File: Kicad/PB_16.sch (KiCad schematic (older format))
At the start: 27 parts, among them J17 Power In Left, J18 Power In Right, J19 USB, J23 VIN_Voltage, J24 Expansion Header, J25 RTC Conn, J26 OLED Select, J27 GPIO Header, J28 Aux Pwr, J29 VIN_Select, SW2 OLED Select, U2 LM7805

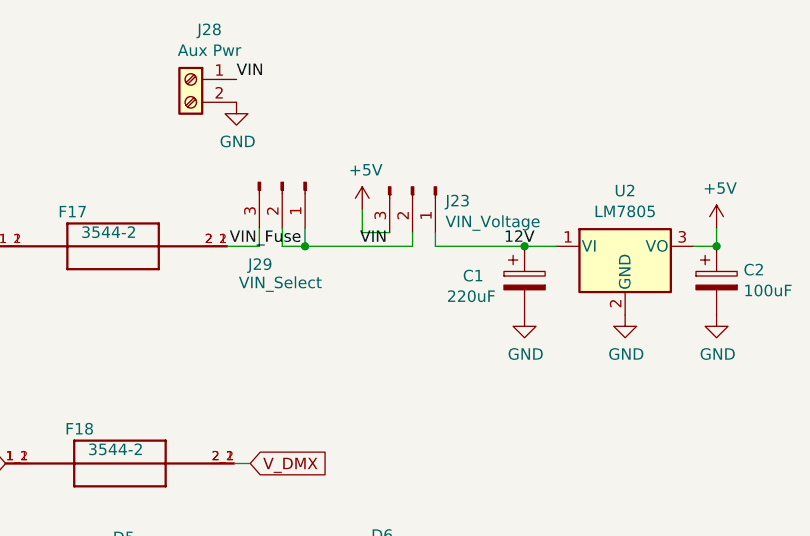
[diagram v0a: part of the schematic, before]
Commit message: updated Aux header to 3.81mm spaced header
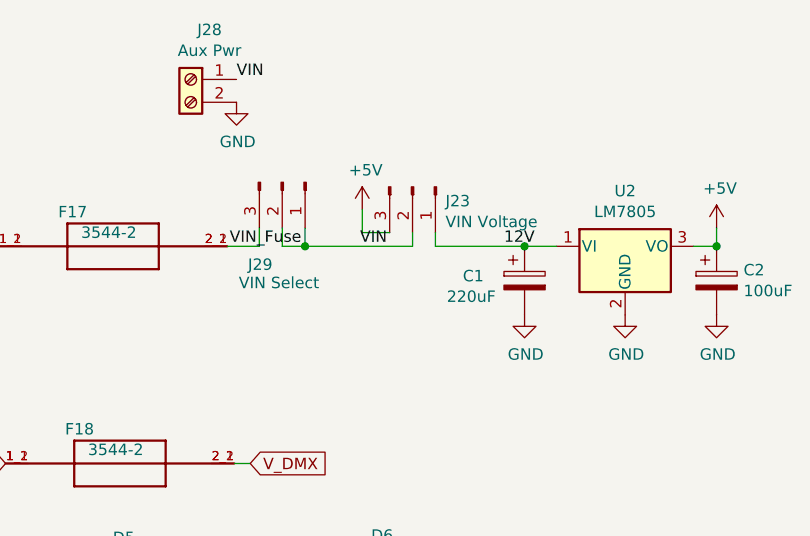
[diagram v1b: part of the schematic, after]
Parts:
- J23: value VIN_Voltage -> VIN Voltage
- J28: footprint TerminalBlock_TE-Connectivity:TerminalBlock_TE_282834-2_1x02_P2.54mm_Horizontal -> TerminalBlock_MetzConnect:TerminalBlock_MetzConnect_Type086_RT03402HBLC_1x02_P3.81mm_Horizontal; Digi-Key_PN A98333-ND -> 277-1947-ND; MPN 282834-2 -> 1727010
- J29: value VIN_Select -> VIN Select
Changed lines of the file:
@@
 EESchema Schematic File Version 4
 LIBS:PB_16-cache
-EELAYER 29 0
+EELAYER 30 0
 EELAYER END
 $Descr A4 11693 8268
@@
 Sheet 1 5
 Title "PB 16"
-Date "2019-08-24"
-Rev "v1.0d"
+Date "2019-09-19"
+Rev "v1.0e"
 Comp "Scott Hanson"
 Comment1 ""
@@
 P 7830 1330
 F 0 "J23" V 7892 1474 50  0000 L CNN
-F 1 "VIN_Voltage" V 7983 1474 50  0000 L CNN
+F 1 "VIN Voltage" V 7983 1474 50  0000 L CNN
 F 2 "Connector_PinHeader_2.54mm:PinHeader_1x03_P2.54mm_Vertical" H 7830 1330 50  0001 C CNN
 F 3 "~" H 7830 1330 50  0001 C CNN
@@
 F 0 "J28" H 6778 1077 50  0000 C CNN
 F 1 "Aux Pwr" H 6778 986 50  0000 C CNN
-F 2 "TerminalBlock_TE-Connectivity:TerminalBlock_TE_282834-2_1x02_P2.54mm_Horizontal" H 6860 860 50  0001 C CNN
+F 2 "TerminalBlock_MetzConnect:TerminalBlock_MetzConnect_Type086_RT03402HBLC_1x02_P3.81mm_Horizontal" H 6860 860 50  0001 C CNN
 F 3 "~" H 6860 860 50  0001 C CNN
-F 4 "A98333-ND" H 6860 860 50  0001 C CNN "Digi-Key_PN"
-F 5 "282834-2" H 6860 860 50  0001 C CNN "MPN"
+F 4 "277-1947-ND" H 6860 860 50  0001 C CNN "Digi-Key_PN"
+F 5 "1727010" H 6860 860 50  0001 C CNN "MPN"
 	1    6860 860
 	-1   0    0    -1
@@
 P 7260 1310
 F 0 "J29" V 7620 1160 50  0000 L CNN
-F 1 "VIN_Select" V 7700 1120 50  0000 L CNN
+F 1 "VIN Select" V 7700 1120 50  0000 L CNN
 F 2 "Connector_PinHeader_2.54mm:PinHeader_1x03_P2.54mm_Vertical" H 7260 1310 50  0001 C CNN
 F 3 "~" H 7260 1310 50  0001 C CNN

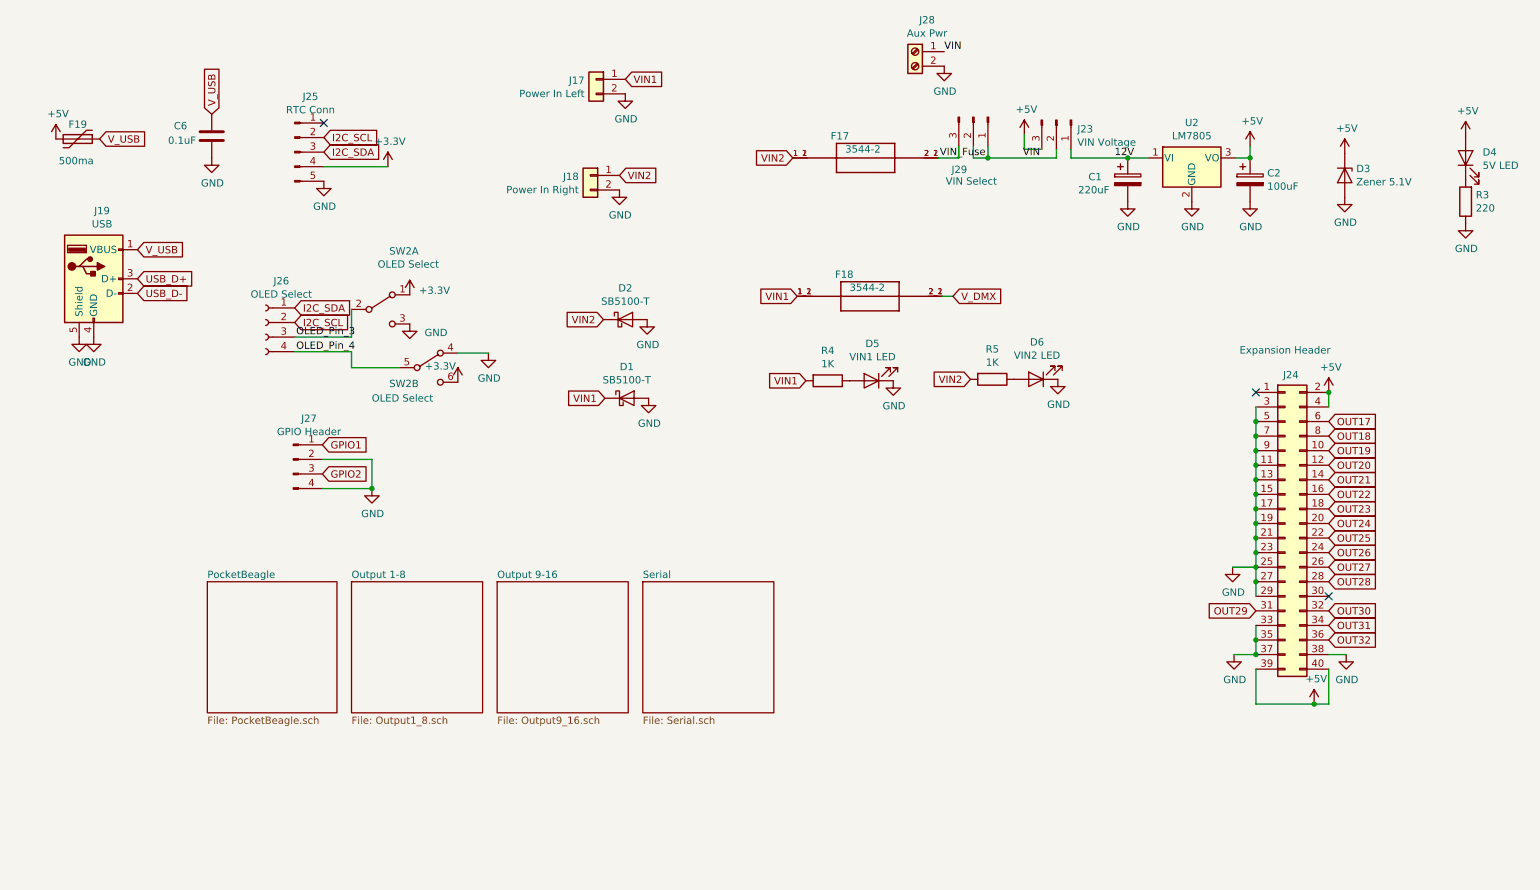
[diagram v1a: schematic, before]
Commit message: Added LOR/DMX Serial Port Selector, EEPROM, and Push buttons
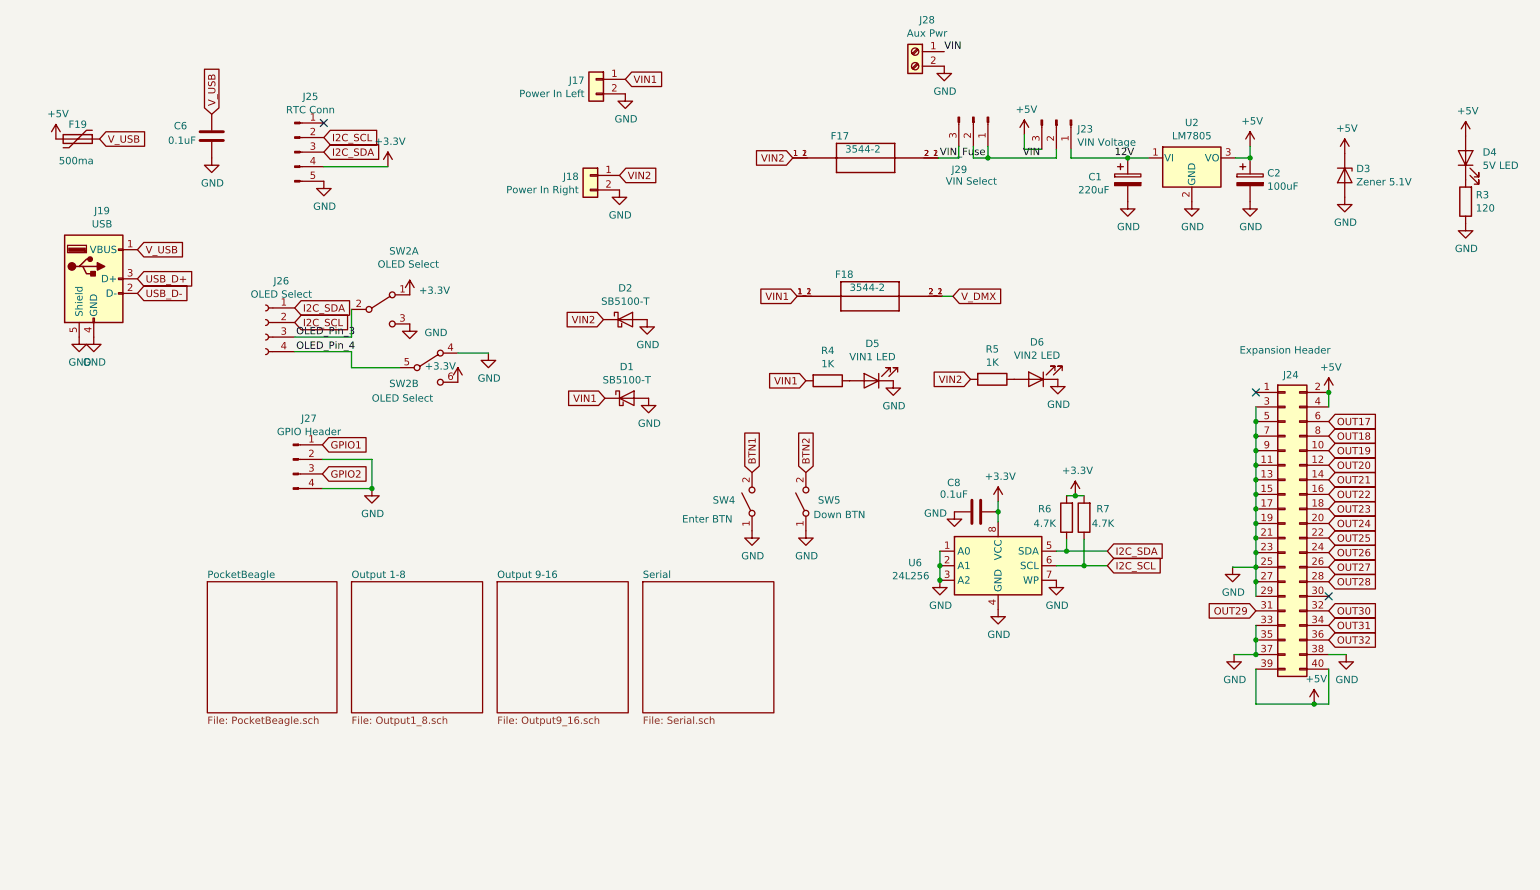
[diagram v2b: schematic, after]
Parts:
- added C8: 0.1uF, Capacitor_THT:C_Rect_L7.0mm_W2.0mm_P5.00mm, symbol Device:C
- added R6, R7: 4.7K, Resistor_THT:R_Axial_DIN0207_L6.3mm_D2.5mm_P7.62mm_Horizontal, symbol Device:R
- added SW4: Enter BTN, Button_Switch_THT:SW_PUSH_6mm, symbol Switch:SW_SPST
- added SW5: Down BTN, Button_Switch_THT:SW_PUSH_6mm, symbol Switch:SW_SPST
- added U6: 24L256, Package_DIP:DIP-8_W7.62mm, symbol Memory_EEPROM:24LC32
- D4, D5, D6: footprint LED_THT:LED_D3.0mm -> LED_THT:LED_D3.0mm_Clear
- R3: value 220 -> 120; Digi-Key_PN CF14JT220RCT-ND -> CF14JT120RCT-ND; MPN CF14JT220R -> CF14JT120R
- U2: footprint Package_TO_SOT_THT:TO-220-3_Horizontal_TabDown -> Package_TO_SOT_THT:TO-220-3_Vertical
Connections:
- net +3V3: now also C8.1, R6.2, R7.2, U6.8 (VCC)
- net GND: now also C8.2, SW4.1 (A), SW5.1 (A), U6.1 (A0), U6.2 (A1), U6.3 (A2), U6.4 (GND), U6.7 (WP)
- net I2C_SCL: now also R7.1, U6.6 (SCL)
- net I2C_SDA: now also R6.1, U6.5 (SDA)
- new net BTN1: SW4.2 (B)
- new net BTN2: SW5.2 (B)
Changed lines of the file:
@@
 Sheet 1 5
 Title "PB 16"
-Date "2019-09-19"
-Rev "v1.0e"
+Date "2019-10-07"
+Rev "v1.0f"
 Comp "Scott Hanson"
 Comment1 ""
@@
 F 0 "U2" H 8760 1832 50  0000 C CNN
 F 1 "LM7805" H 8760 1741 50  0000 C CNN
-F 2 "Package_TO_SOT_THT:TO-220-3_Horizontal_TabDown" H 8760 1815 50  0001 C CIN
+F 2 "Package_TO_SOT_THT:TO-220-3_Vertical" H 8760 1815 50  0001 C CIN
 F 3 "http://www.fairchildsemi.com/ds/LM/LM7805.pdf" H 8760 1540 50  0001 C CNN
 F 4 "811-2196-5-ND" H -340 -170 50  0001 C CNN "Digi-Key_PN"
@@
 F 0 "D5" H 6553 2865 50  0000 C CNN
 F 1 "VIN1 LED" H 6553 2956 50  0000 C CNN
-F 2 "LED_THT:LED_D3.0mm" H 6560 3120 50  0001 C CNN
+F 2 "LED_THT:LED_D3.0mm_Clear" H 6560 3120 50  0001 C CNN
 F 3 "~" H 6560 3120 50  0001 C CNN
 F 4 "754-1217-ND" H 6560 3120 50  0001 C CNN "Digi-Key_PN"
@@
 P 10640 1890
 F 0 "R3" H 10570 1844 50  0000 R CNN
-F 1 "220" H 10570 1935 50  0000 R CNN
+F 1 "120" H 10570 1935 50  0000 R CNN
 F 2 "Resistor_THT:R_Axial_DIN0207_L6.3mm_D2.5mm_P7.62mm_Horizontal" V 10570 1890 50  0001 C CNN
 F 3 "~" H 10640 1890 50  0001 C CNN
-F 4 "CF14JT220RCT-ND" H 10640 1890 50  0001 C CNN "Digi-Key_PN"
-F 5 "CF14JT220R" H 10640 1890 50  0001 C CNN "MPN"
+F 4 "CF14JT120RCT-ND" H 10640 1890 50  0001 C CNN "Digi-Key_PN"
+F 5 "CF14JT120R" H 10640 1890 50  0001 C CNN "MPN"
 	1    10640 1890
 	-1   0    0    1
@@
 F 0 "D6" H 7683 2855 50  0000 C CNN
 F 1 "VIN2 LED" H 7683 2946 50  0000 C CNN
-F 2 "LED_THT:LED_D3.0mm" H 7690 3110 50  0001 C CNN
+F 2 "LED_THT:LED_D3.0mm_Clear" H 7690 3110 50  0001 C CNN
 F 3 "~" H 7690 3110 50  0001 C CNN
 F 4 "754-1217-ND" H 7690 3110 50  0001 C CNN "Digi-Key_PN"
@@
 F 0 "D4" V 10679 1473 50  0000 R CNN
 F 1 "5V LED" V 10588 1473 50  0000 R CNN
-F 2 "LED_THT:LED_D3.0mm" H 10640 1590 50  0001 C CNN
+F 2 "LED_THT:LED_D3.0mm_Clear" H 10640 1590 50  0001 C CNN
 F 3 "~" H 10640 1590 50  0001 C CNN
 F 4 "754-1217-ND" H 10640 1590 50  0001 C CNN "Digi-Key_PN"
@@
 Wire Wire Line
 	7360 1510 7360 1590
+$Comp
+L Memory_EEPROM:24LC32 U6
+U 1 1 5D915A6B
+P 7430 4390
+F 0 "U6" H 6860 4410 50  0000 C CNN
+F 1 "24L256" H 6830 4320 50  0000 C CNN
+F 2 "Package_DIP:DIP-8_W7.62mm" H 7430 4390 50  0001 C CNN
+F 3 "http://ww1.microchip.com/downloads/en/DeviceDoc/21072G.pdf" H 7430 4390 50  0001 C CNN
+F 4 "1219-1052-ND" H 7430 4390 50  0001 C CNN "Digi-Key_PN"
+F 5 "FT24C256A-UDR-B" H 7430 4390 50  0001 C CNN "MPN"
+	1    7430 4390
+	1    0    0    -1
+$EndComp
+$Comp
+L power:GND #PWR059
+U 1 1 5D917DF1
+P 7830 4490
+F 0 "#PWR059" H 7830 4240 50  0001 C CNN
+F 1 "GND" H 7835 4317 50  0000 C CNN
+F 2 "" H 7830 4490 50  0001 C CNN
+F 3 "" H 7830 4490 50  0001 C CNN
+	1    7830 4490
+	1    0    0    -1
+$EndComp
+Text GLabel 8180 4390 2    50   Input ~ 0
+I2C_SCL
+Text GLabel 8180 4290 2    50   Input ~ 0
+I2C_SDA
+$Comp
+L power:+3.3V #PWR?
+U 1 1 5D918D0A
+P 7430 3950
+AR Path="/5D413C25/5D918D0A" Ref="#PWR?"  Part="1"
+AR Path="/5D918D0A" Ref="#PWR057"  Part="1"
+F 0 "#PWR057" H 7430 3800 50  0001 C CNN
+F 1 "+3.3V" H 7445 4123 50  0000 C CNN
+F 2 "" H 7430 3950 50  0001 C CNN
+F 3 "" H 7430 3950 50  0001 C CNN
+	1    7430 3950
+	1    0    0    -1
+$EndComp
+$Comp
+L power:GND #PWR058
+U 1 1 5D91A827
+P 7430 4690
+F 0 "#PWR058" H 7430 4440 50  0001 C CNN
+F 1 "GND" H 7435 4517 50  0000 C CNN
+F 2 "" H 7430 4690 50  0001 C CNN
+F 3 "" H 7430 4690 50  0001 C CNN
+	1    7430 4690
+	1    0    0    -1
+$EndComp
+$Comp
+L power:GND #PWR056
+U 1 1 5D91AC52
+P 7130 4020
+F 0 "#PWR056" H 7130 3770 50  0001 C CNN
+F 1 "GND" H 7000 4010 50  0000 C CNN
+F 2 "" H 7130 4020 50  0001 C CNN
+F 3 "" H 7130 4020 50  0001 C CNN
+	1    7130 4020
+	1    0    0    -1
+$EndComp
+Wire Wire Line
+	7030 4290 7030 4390
+Connection ~ 7030 4390
+Wire Wire Line
+	7030 4390 7030 4490
+Wire Wire Line
+	7830 4290 7900 4290
+Wire Wire Line
+	8180 4390 8020 4390
+$Comp
+L Device:C C?
+U 1 1 5D91E5B7
+P 7280 4020
+AR Path="/5D413C25/5D91E5B7" Ref="C?"  Part="1"
+AR Path="/5D91E5B7" Ref="C8"  Part="1"
+F 0 "C8" V 7080 3820 50  0000 L CNN
+F 1 "0.1uF" V 7160 3770 50  0000 L CNN
+F 2 "Capacitor_THT:C_Rect_L7.0mm_W2.0mm_P5.00mm" H 7318 3870 50  0001 C CNN
+F 3 "~" H 7280 4020 50  0001 C CNN
+F 4 "478-7336-1-ND" H 7280 4020 50  0001 C CNN "Digi-Key_PN"
+F 5 "SR215C104KARTR1" H 7280 4020 50  0001 C CNN "MPN"
+	1    7280 4020
+	0    1    1    0
+$EndComp
+Wire Wire Line
+	7430 4090 7430 4020
+Connection ~ 7430 4020
+Wire Wire Line
+	7430 4020 7430 3950
+$Comp
+L Device:R R6
+U 1 1 5D925D1A
+P 7900 4060
+F 0 "R6" H 8050 4000 50  0000 C CNN
+F 1 "4.7K" H 8050 4100 50  0000 C CNN
+F 2 "Resistor_THT:R_Axial_DIN0207_L6.3mm_D2.5mm_P7.62mm_Horizontal" V 7830 4060 50  0001 C CNN
+F 3 "~" H 7900 4060 50  0001 C CNN
+F 4 "CF14JT4K70CT-ND" H 7900 4060 50  0001 C CNN "Digi-Key_PN"
+F 5 "CF14JT4K70" H 7900 4060 50  0001 C CNN "MPN"
+	1    7900 4060
+	-1   0    0    1
+$EndComp
+$Comp
+L Device:R R7
+U 1 1 5D9267BC
+P 8020 4060
+F 0 "R7" H 7890 4000 50  0000 C CNN
+F 1 "4.7K" H 7890 4100 50  0000 C CNN
+F 2 "Resistor_THT:R_Axial_DIN0207_L6.3mm_D2.5mm_P7.62mm_Horizontal" V 7950 4060 50  0001 C CNN
+F 3 "~" H 8020 4060 50  0001 C CNN
+F 4 "CF14JT4K70CT-ND" H 8020 4060 50  0001 C CNN "Digi-Key_PN"
+F 5 "CF14JT4K70" H 8020 4060 50  0001 C CNN "MPN"
+	1    8020 4060
+	-1   0    0    1
+$EndComp
+$Comp
+L power:+3.3V #PWR?
+U 1 1 5D926B37
+P 7960 3910
+AR Path="/5D413C25/5D926B37" Ref="#PWR?"  Part="1"
+AR Path="/5D926B37" Ref="#PWR060"  Part="1"
+F 0 "#PWR060" H 7960 3760 50  0001 C CNN
+F 1 "+3.3V" H 7975 4083 50  0000 C CNN
+F 2 "" H 7960 3910 50  0001 C CNN
+F 3 "" H 7960 3910 50  0001 C CNN
+	1    7960 3910
+	1    0    0    -1
+$EndComp
+Wire Wire Line
+	7900 3910 7960 3910
+Connection ~ 7960 3910
+Wire Wire Line
+	7960 3910 8020 3910
+Wire Wire Line
+	7900 4210 7900 4290
+Connection ~ 7900 4290
+Wire Wire Line
+	7900 4290 8180 4290
+Wire Wire Line
+	8020 4210 8020 4390
+Connection ~ 8020 4390
+Wire Wire Line
+	8020 4390 7830 4390
+$Comp
+L power:GND #PWR0118
+U 1 1 5D92B95E
+P 7030 4490
+F 0 "#PWR0118" H 7030 4240 50  0001 C CNN
+F 1 "GND" H 7035 4317 50  0000 C CNN
+F 2 "" H 7030 4490 50  0001 C CNN
+F 3 "" H 7030 4490 50  0001 C CNN
+	1    7030 4490
+	1    0    0    -1
+$EndComp
+Connection ~ 7030 4490
+$Comp
+L Switch:SW_SPST SW4
+U 1 1 5DA38F90
+P 5740 3950
+F 0 "SW4" V 5750 4220 50  0000 R CNN
+F 1 "Enter BTN" V 5620 4430 50  0000 R CNN
+F 2 "Button_Switch_THT:SW_PUSH_6mm" H 5740 3950 50  0001 C CNN
+F 3 "~" H 5740 3950 50  0001 C CNN
+F 4 "450-1650-ND" H 5740 3950 50  0001 C CNN "Digi-Key_PN"
+F 5 "1825910-6" H 5740 3950 50  0001 C CNN "MPN"
+	1    5740 3950
+	0    -1   -1   0
+$EndComp
+$Comp
+L Switch:SW_SPST SW5
+U 1 1 5DA3A295
+P 6110 3950
+F 0 "SW5" V 6120 3790 50  0000 C CNN
+F 1 "Down BTN" V 6020 3720 50  0000 C CNN
+F 2 "Button_Switch_THT:SW_PUSH_6mm" H 6110 3950 50  0001 C CNN
+F 3 "~" H 6110 3950 50  0001 C CNN
+F 4 "450-1650-ND" H 6110 3950 50  0001 C CNN "Digi-Key_PN"
+F 5 "1825910-6" H 6110 3950 50  0001 C CNN "MPN"
+	1    6110 3950
+	0    -1   -1   0
+$EndComp
+$Comp
+L power:GND #PWR0119
+U 1 1 5DA6DBF7
+P 5740 4150
+F 0 "#PWR0119" H 5740 3900 50  0001 C CNN
+F 1 "GND" H 5745 3977 50  0000 C CNN
+F 2 "" H 5740 4150 50  0001 C CNN
+F 3 "" H 5740 4150 50  0001 C CNN
+	1    5740 4150
+	1    0    0    -1
+$EndComp
+$Comp
+L power:GND #PWR0120
+U 1 1 5DA6E312
+P 6110 4150
+F 0 "#PWR0120" H 6110 3900 50  0001 C CNN
+F 1 "GND" H 6115 3977 50  0000 C CNN
+F 2 "" H 6110 4150 50  0001 C CNN
+F 3 "" H 6110 4150 50  0001 C CNN
+	1    6110 4150
+	1    0    0    -1
+$EndComp
+Text GLabel 5740 3750 1    50   Input ~ 0
+BTN1
+Text GLabel 6110 3750 1    50   Input ~ 0
+BTN2
 $EndSCHEMATC

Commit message: fixed aux header
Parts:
- J28: footprint TerminalBlock_MetzConnect:TerminalBlock_MetzConnect_Type086_RT03402HBLC_1x02_P3.81mm_Horizontal -> MKDS1_2-3.81:PHOENIX_MKDS1%2f2-3.81
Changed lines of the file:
@@
 F 0 "J28" H 6778 1077 50  0000 C CNN
 F 1 "Aux Pwr" H 6778 986 50  0000 C CNN
-F 2 "TerminalBlock_MetzConnect:TerminalBlock_MetzConnect_Type086_RT03402HBLC_1x02_P3.81mm_Horizontal" H 6860 860 50  0001 C CNN
+F 2 "MKDS1_2-3.81:PHOENIX_MKDS1%2f2-3.81" H 6860 860 50  0001 C CNN
 F 3 "~" H 6860 860 50  0001 C CNN
 F 4 "277-1947-ND" H 6860 860 50  0001 C CNN "Digi-Key_PN"

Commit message: updated PB16 to rev G, changed power in ports to screw type connector
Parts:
- J17, J18: footprint TerminalBlock_MetzConnect:TerminalBlock_MetzConnect_Type701_RT11L02HGLU_1x02_P6.35mm_Horizontal -> Barrier_Blocks:BARRIER_BLOCK_1ROW_2POS_P9.5MM; symbol Connector_Generic:Conn_01x02 -> Barrier_Blocks:BARRIER_BLOCK_1ROW_2POS; Digi-Key_PN ED2675-ND -> ED2953-ND; MPN OSTT7020150 -> OSTYK51102030
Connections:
- net GND: now also J17.1 (P1); no longer J17.2 (Pin_2)
- net VIN1: now also J17.2 (P2); no longer J17.1 (Pin_1)
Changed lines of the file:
@@
 EESchema Schematic File Version 4
-LIBS:PB_16-cache
 EELAYER 30 0
 EELAYER END
@@
 Sheet 1 5
 Title "PB 16"
-Date "2019-10-07"
-Rev "v1.0f"
+Date "2020-05-09"
+Rev "v1.0g"
 Comp "Scott Hanson"
 Comment1 ""
@@
 Comment4 ""
 $EndDescr
-$Comp
-L Connector_Generic:Conn_01x02 J17
-U 1 1 5CEC911C
-P 4670 1050
-F 0 "J17" H 4750 1042 50  0000 L CNN
-F 1 "Power In Left" H 4750 951 50  0000 L CNN
-F 2 "TerminalBlock_MetzConnect:TerminalBlock_MetzConnect_Type701_RT11L02HGLU_1x02_P6.35mm_Horizontal" H 4670 1050 50  0001 C CNN
-F 3 "~" H 4670 1050 50  0001 C CNN
-F 4 "ED2675-ND" H -3850 190 50  0001 C CNN "Digi-Key_PN"
-F 5 "OSTT7020150" H -3850 190 50  0001 C CNN "MPN"
-	1    4670 1050
-	-1   0    0    -1
-$EndComp
 $Comp
 L Regulator_Linear:LM7805_TO220 U2
@@
 L power:GND #PWR0101
 U 1 1 5CED08B0
-P 4870 1150
-F 0 "#PWR0101" H 4870 900 50  0001 C CNN
-F 1 "GND" H 4875 977 50  0000 C CNN
-F 2 "" H 4870 1150 50  0001 C CNN
-F 3 "" H 4870 1150 50  0001 C CNN
-	1    4870 1150
+P 5020 1150
+F 0 "#PWR0101" H 5020 900 50  0001 C CNN
+F 1 "GND" H 5025 977 50  0000 C CNN
+F 2 "" H 5020 1150 50  0001 C CNN
+F 3 "" H 5020 1150 50  0001 C CNN
+	1    5020 1150
 	1    0    0    -1
 $EndComp
@@
 $EndSheet
 $Comp
-L Connector_Generic:Conn_01x02 J18
+L Barrier_Blocks:BARRIER_BLOCK_1ROW_2POS J18
 U 1 1 5D51C5DD
 P 4630 1710
-F 0 "J18" H 4710 1702 50  0000 L CNN
-F 1 "Power In Right" H 4710 1611 50  0000 L CNN
-F 2 "TerminalBlock_MetzConnect:TerminalBlock_MetzConnect_Type701_RT11L02HGLU_1x02_P6.35mm_Horizontal" H 4630 1710 50  0001 C CNN
+F 0 "J18" H 4790 1710 50  0000 L CNN
+F 1 "Power In Right" H 4760 1610 50  0000 L CNN
+F 2 "Barrier_Blocks:BARRIER_BLOCK_1ROW_2POS_P9.5MM" H 4630 1710 50  0001 C CNN
 F 3 "~" H 4630 1710 50  0001 C CNN
-F 4 "ED2675-ND" H -3890 850 50  0001 C CNN "Digi-Key_PN"
-F 5 "OSTT7020150" H -3890 850 50  0001 C CNN "MPN"
+F 4 "ED2953-ND" H -3890 850 50  0001 C CNN "Digi-Key_PN"
+F 5 "OSTYK51102030" H -3890 850 50  0001 C CNN "MPN"
 	1    4630 1710
 	-1   0    0    -1
@@
 L power:GND #PWR02
 U 1 1 5D51C5E3
-P 4830 1810
-F 0 "#PWR02" H 4830 1560 50  0001 C CNN
-F 1 "GND" H 4835 1637 50  0000 C CNN
-F 2 "" H 4830 1810 50  0001 C CNN
-F 3 "" H 4830 1810 50  0001 C CNN
-	1    4830 1810
-	1    0    0    -1
-$EndComp
-Text GLabel 4830 1710 2    50   Input ~ 0
+P 4980 1810
+F 0 "#PWR02" H 4980 1560 50  0001 C CNN
+F 1 "GND" H 4985 1637 50  0000 C CNN
+F 2 "" H 4980 1810 50  0001 C CNN
+F 3 "" H 4980 1810 50  0001 C CNN
+	1    4980 1810
+	1    0    0    -1
+$EndComp
+Text GLabel 4980 1610 2    50   Input ~ 0
 VIN2
-Text GLabel 4870 1050 2    50   Input ~ 0
+Text GLabel 5020 950  2    50   Input ~ 0
 VIN1
 Text GLabel 6020 1590 0    50   Input ~ 0
@@
 Text GLabel 6110 3750 1    50   Input ~ 0
 BTN2
+$Comp
+L Barrier_Blocks:BARRIER_BLOCK_1ROW_2POS J17
+U 1 1 5CEC911C
+P 4670 1050
+F 0 "J17" H 4810 1050 50  0000 L CNN
+F 1 "Power In Left" H 4790 935 50  0000 L CNN
+F 2 "Barrier_Blocks:BARRIER_BLOCK_1ROW_2POS_P9.5MM" H 4670 1050 50  0001 C CNN
+F 3 "~" H 4670 1050 50  0001 C CNN
+F 4 "ED2953-ND" H -3850 190 50  0001 C CNN "Digi-Key_PN"
+F 5 "OSTYK51102030" H -3850 190 50  0001 C CNN "MPN"
+	1    4670 1050
+	-1   0    0    1
+$EndComp
 $EndSCHEMATC
